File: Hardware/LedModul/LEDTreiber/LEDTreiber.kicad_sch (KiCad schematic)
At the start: 15 parts, among them J1 Conn_01x01_Pin, J2 Conn_01x01_Pin, J3 Conn_01x01_Pin, J4 Conn_01x01_Pin, J5 Conn_01x01_Pin, U1 TPS92200DxRXL, U2 TVS2700DRV

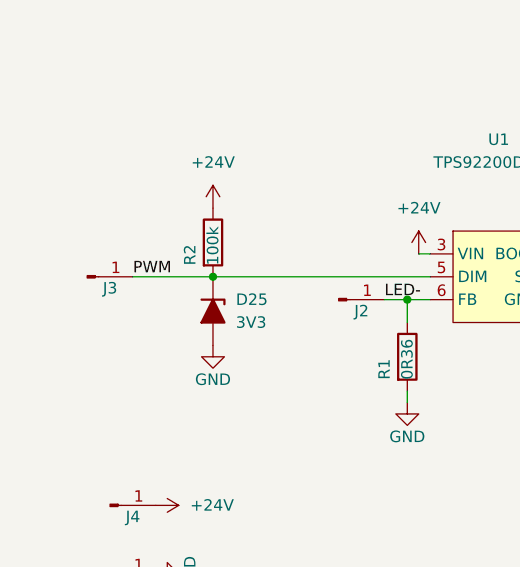
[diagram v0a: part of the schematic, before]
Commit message: PogoPin pcb added
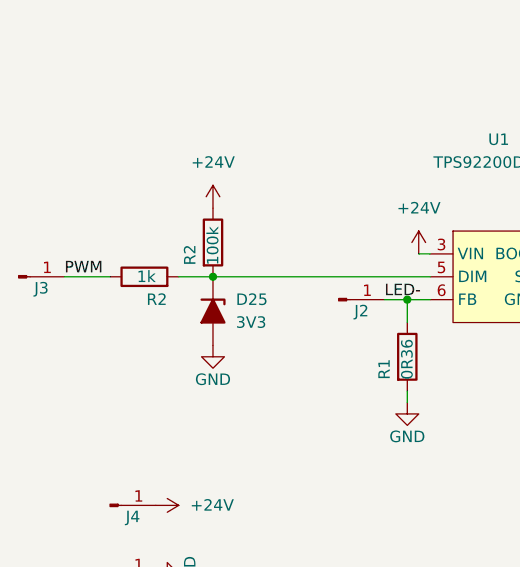
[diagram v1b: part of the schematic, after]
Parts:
- added R2: 1k, Resistor_SMD:R_0603_1608Metric, symbol Device:R
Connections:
- net PWM: now also R2.1; no longer D25.1 (K), R2.2, U1.5 (DIM)
- new net: D25.1 (K), R2.2, R2.2, U1.5 (DIM)
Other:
- moved on the sheet: J3
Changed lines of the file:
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@@
-    (stroke (width 0) (type default))
-  )
-  (wire (pts (xy 130.81 87.63) (xy 139.7 87.63))
     (stroke (width 0) (type default))
   )
@@
     (stroke (width 0) (type default))
   )
+  (wire (pts (xy 135.89 87.63) (xy 139.7 87.63))
+    (stroke (width 0) (type default))
+  )
   (wire (pts (xy 186.69 87.63) (xy 186.69 82.55))
     (stroke (width 0) (type default))
   )
   (wire (pts (xy 158.75 90.17) (xy 161.29 90.17))
+    (stroke (width 0) (type default))
+  )
+  (wire (pts (xy 123.19 87.63) (xy 128.27 87.63))
     (stroke (width 0) (type default))
   )
@@
     (effects (font (size 1.27 1.27)) (justify left bottom))
   )
-  (label "PWM" (at 130.81 87.63 0) (fields_autoplaced)
+  (label "PWM" (at 123.19 87.63 0) (fields_autoplaced)
     (effects (font (size 1.27 1.27)) (justify left bottom))
   )
@@
     )
   )
-  (symbol (lib_id "Connector:Conn_01x01_Pin") (at 125.73 87.63 0) (unit 1)
-    (in_bom yes) (on_board yes) (dnp no)
-    (property "Reference" "J3" (at 128.27 88.9 0)
-      (effects (font (size 1.27 1.27)))
-    )
-    (property "Value" "Conn_01x01_Pin" (at 126.365 90.17 0)
-      (effects (font (size 1.27 1.27)) hide)
-    )
-    (property "Footprint" "TestPoint:TestPoint_Pad_D2.0mm" (at 125.73 87.63 0)
-      (effects (font (size 1.27 1.27)) hide)
-    )
-    (property "Datasheet" "~" (at 125.73 87.63 0)
+  (symbol (lib_id "Connector:Conn_01x01_Pin") (at 118.11 87.63 0) (unit 1)
+    (in_bom yes) (on_board yes) (dnp no)
+    (property "Reference" "J3" (at 120.65 88.9 0)
+      (effects (font (size 1.27 1.27)))
+    )
+    (property "Value" "Conn_01x01_Pin" (at 118.745 90.17 0)
+      (effects (font (size 1.27 1.27)) hide)
+    )
+    (property "Footprint" "TestPoint:TestPoint_Pad_D2.0mm" (at 118.11 87.63 0)
+      (effects (font (size 1.27 1.27)) hide)
+    )
+    (property "Datasheet" "~" (at 118.11 87.63 0)
       (effects (font (size 1.27 1.27)) hide)
     )
@@
         )
       )
+    )
+  )
+  (symbol (lib_id "Device:R") (at 132.08 87.63 90) (unit 1)
+    (in_bom yes) (on_board yes) (dnp no)
+    (property "Reference" "R2" (at 134.62 90.17 90)
+      (effects (font (size 1.27 1.27)) (justify left))
+    )
+    (property "Value" "1k" (at 133.35 87.63 90)
+      (effects (font (size 1.27 1.27)) (justify left))
+    )
+    (property "Footprint" "Resistor_SMD:R_0603_1608Metric" (at 132.08 89.408 90)
+      (effects (font (size 1.27 1.27)) hide)
+    )
+    (property "Datasheet" "~" (at 132.08 87.63 0)
+      (effects (font (size 1.27 1.27)) hide)
+    )
+    (pin "1")
+    (pin "2")
+    (instances
+      (project "Treiber"
+        (path "/c3a2acff-1485-499a-b84f-a6a115b6f0c8"
+          (reference "R2") (unit 1)
+        )
+      )
+      (project "LEDTreiber"
+        (path "/d82ce847-78d6-4fa0-8b73-8d8851ed8da0"
+          (reference "R3") (unit 1)
+        )
+      )

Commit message: V1.1
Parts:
- J1, J2: footprint Bergi:Solderpad_1x2 -> Connector_PinHeader_2.54mm:PinHeader_1x01_P2.54mm_Vertical
- R2: value 100k -> 1M
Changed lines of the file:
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@@
       (effects (font (size 1.27 1.27)) hide)
     )
-    (property "Footprint" "Bergi:Solderpad_1x2" (at 205.74 87.63 0)
+    (property "Footprint" "Connector_PinHeader_2.54mm:PinHeader_1x01_P2.54mm_Vertical" (at 205.74 87.63 0)
       (effects (font (size 1.27 1.27)) hide)
     )
@@
       (effects (font (size 1.27 1.27)) hide)
     )
-    (property "Footprint" "Bergi:Solderpad_1x2" (at 153.67 90.17 0)
+    (property "Footprint" "Connector_PinHeader_2.54mm:PinHeader_1x01_P2.54mm_Vertical" (at 153.67 90.17 0)
       (effects (font (size 1.27 1.27)) hide)
     )
@@
       (effects (font (size 1.27 1.27)) (justify left))
     )
-    (property "Value" "100k" (at 139.7 86.36 90)
-      (effects (font (size 1.27 1.27)) (justify left))
-    )
+    (property "Value" "1M" (at 139.7 86.36 90)
+      (effects (font (size 1.27 1.27)) (justify left))
+    )
